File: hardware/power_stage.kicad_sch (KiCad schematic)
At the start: 30 parts, among them J10 Phase A, J11 Phase B, J12 Phase C, Q1 ISC022N10NM6, Q2 ISC022N10NM6, Q3 ISC022N10NM6, Q4 ISC022N10NM6, Q5 ISC022N10NM6, Q6 ISC022N10NM6

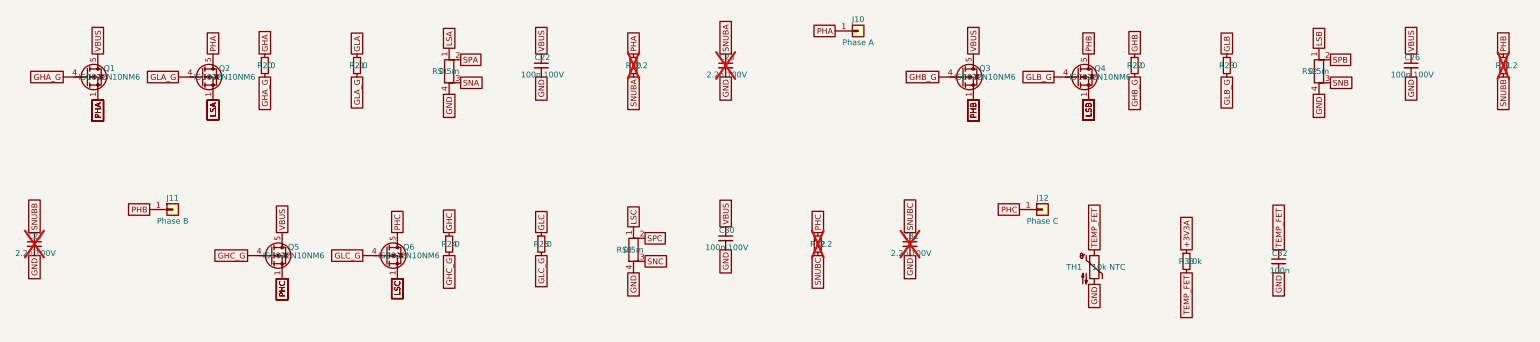
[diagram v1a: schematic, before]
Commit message: Layout rev B: top-side two-shunt power stage, 5.0SMDJ60A TVS, crystal by the MCU
Commutation loop 5.0 -> 3.0 nH (FastHenry), 60 V hot-plug peak 106 -> 96 V.
Re-placed and re-routed (Freerouting + tools/hand_route.py); DRC: 0 unconnected,
only the MD80-inherent AUX1/screw courtyard overlap. Docs and sims updated.

Co-Authored-By: Claude Opus 5.5 (1M context) <noreply@anthropic.com>
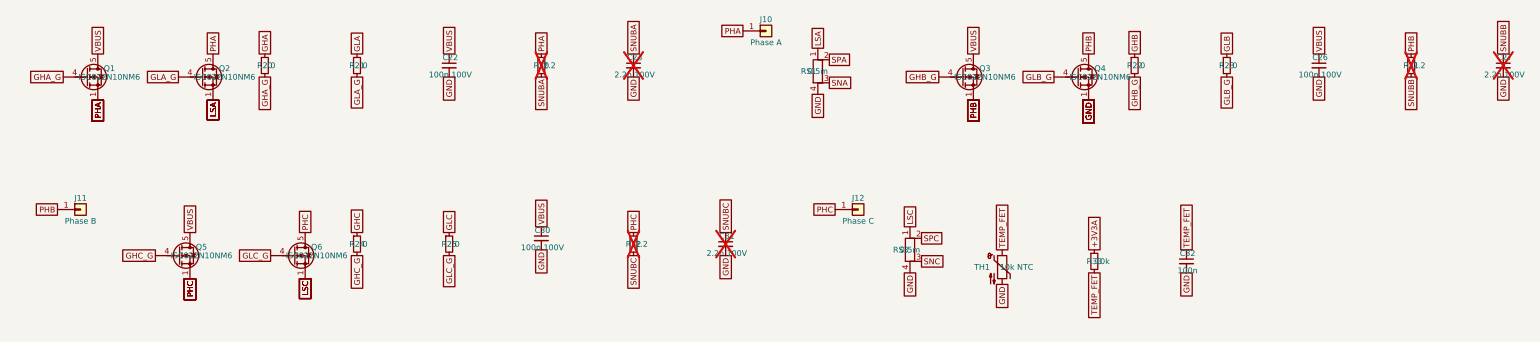
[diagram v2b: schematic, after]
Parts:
- removed RS2: 0.5m, Resistor_SMD:R_Shunt_Vishay_WSK2512_6332Metric_T2.66mm, symbol Device:R_Shunt
- R30, R31, R32: footprint Resistor_SMD:R_0805_2012Metric -> Resistor_SMD:R_1206_3216Metric; Note RC snubber, fit if needed -> RC snubber; fit on first boards (sim/double_pulse.py), 0.3 W
- RS1, RS3: Note Kelvin 4-terminal; other series need a footprint change -> Kelvin 4-terminal, top side between the FETs
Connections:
- net LSB is gone; now on net GND: Q4.1 (S), Q4.2 (S), Q4.3 (S)
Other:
- moved on the sheet: C22, C23, C26, C27, C30, C31, C32, J10, J11, J12, Q5, Q6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
